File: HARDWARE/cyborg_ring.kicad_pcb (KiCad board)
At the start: 2 copper layers, 45 x 24.6 mm, 43 parts, among them SW1 SW_PUSH, U1 ATtiny85_QFN20_1-5, U2 ATtiny85_QFN20_11-15

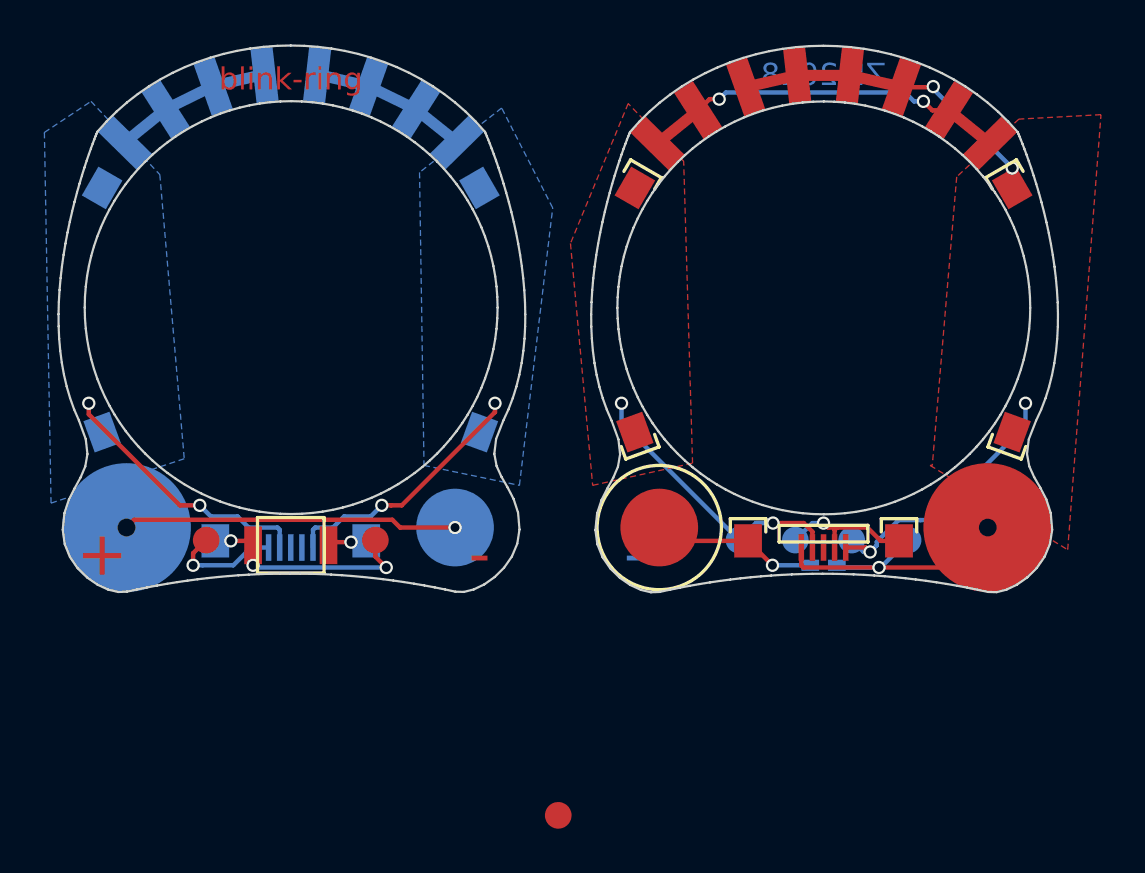
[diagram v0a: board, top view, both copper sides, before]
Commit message: localized schematic symbols. changed name. minor formatting changes.
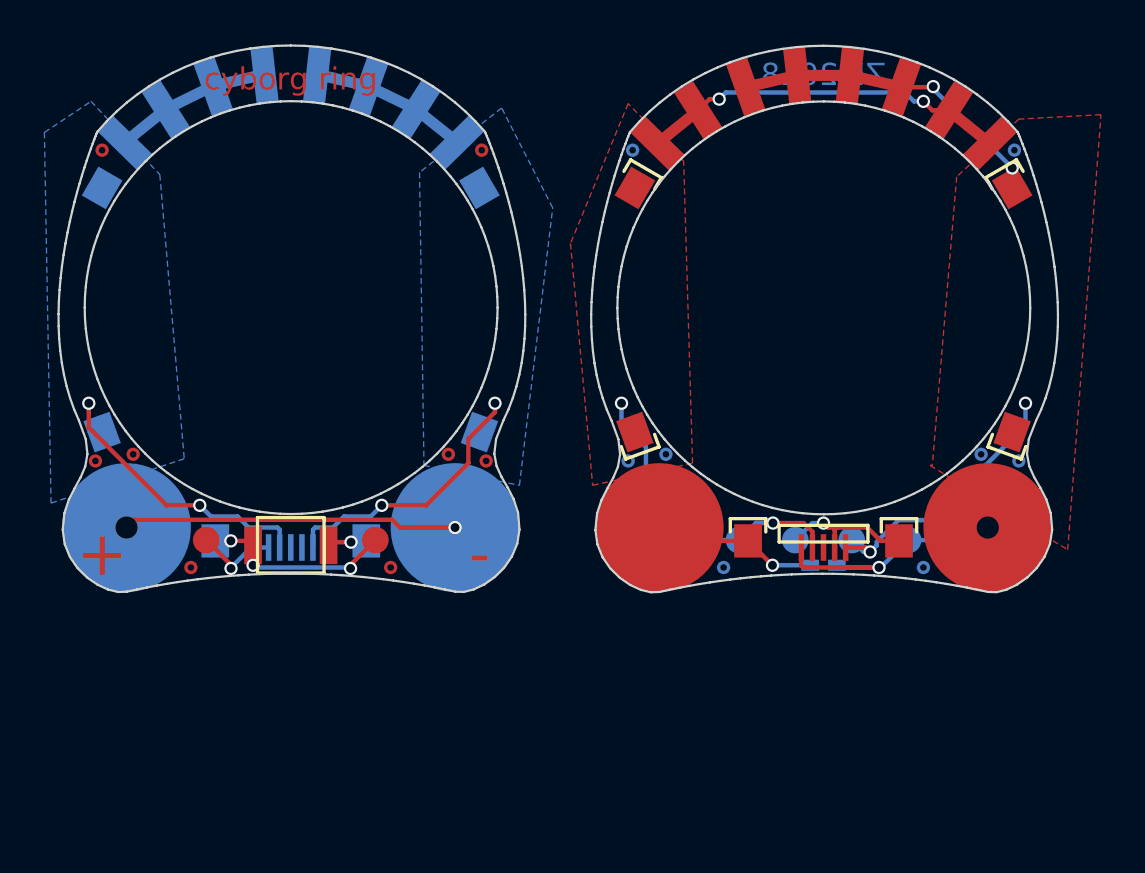
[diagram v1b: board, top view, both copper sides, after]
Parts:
- removed TP6: GND, KiCad_Footprints:ZF_CONN_1-2_pad
- added REF**: ZF_STRUCT_HOLE_0-30mm, KiCad_Footprints:ZF_STRUCT_HOLE_0-30mm, B.Cu at (98.6, 132.8)
- added REF**: ZF_STRUCT_HOLE_0-30mm, KiCad_Footprints:ZF_STRUCT_HOLE_0-30mm, F.Cu at (57.2, 146.8)
- added REF**: ZF_STRUCT_HOLE_0-30mm, KiCad_Footprints:ZF_STRUCT_HOLE_0-30mm, F.Cu at (58.9, 146.5)
- added REF**: ZF_STRUCT_HOLE_0-30mm, KiCad_Footprints:ZF_STRUCT_HOLE_0-30mm, F.Cu at (73.1, 146.5)
- added REF**: ZF_STRUCT_HOLE_0-30mm, KiCad_Footprints:ZF_STRUCT_HOLE_0-30mm, F.Cu at (74.8, 146.8)
- added REF**: ZF_STRUCT_HOLE_0-30mm, KiCad_Footprints:ZF_STRUCT_HOLE_0-30mm, B.Cu at (81.2, 146.8)
- added REF**: ZF_STRUCT_HOLE_0-30mm, KiCad_Footprints:ZF_STRUCT_HOLE_0-30mm, B.Cu at (82.9, 146.5)
- added REF**: ZF_STRUCT_HOLE_0-30mm, KiCad_Footprints:ZF_STRUCT_HOLE_0-30mm, B.Cu at (98.8, 146.8)
- added REF**: ZF_STRUCT_HOLE_0-30mm, KiCad_Footprints:ZF_STRUCT_HOLE_0-30mm, B.Cu at (97.1, 146.5)
- added REF**: ZF_STRUCT_HOLE_0-30mm, KiCad_Footprints:ZF_STRUCT_HOLE_0-30mm, F.Cu at (57.5, 132.8)
- added REF**: ZF_STRUCT_HOLE_0-30mm, KiCad_Footprints:ZF_STRUCT_HOLE_0-30mm, F.Cu at (74.6, 132.8)
- added REF**: ZF_STRUCT_HOLE_0-30mm, KiCad_Footprints:ZF_STRUCT_HOLE_0-30mm, B.Cu at (81.4, 132.8)
- added REF**: ZF_STRUCT_HOLE_0-30mm, KiCad_Footprints:ZF_STRUCT_HOLE_0-30mm, F.Cu at (61.5, 151.6)
- added REF**: ZF_STRUCT_HOLE_0-30mm, KiCad_Footprints:ZF_STRUCT_HOLE_0-30mm, F.Cu at (70.5, 151.6)
- added REF**: ZF_STRUCT_HOLE_0-30mm, KiCad_Footprints:ZF_STRUCT_HOLE_0-30mm, B.Cu at (85.5, 151.6)
- added REF**: ZF_STRUCT_HOLE_0-30mm, KiCad_Footprints:ZF_STRUCT_HOLE_0-30mm, B.Cu at (94.5, 151.6)
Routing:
- net VCC: track 13.7 -> 11.9 mm
- net Net-(NA3-Pad1): track 10.2 -> 8.88 mm
- net Net-(TP1-Pad1): track 5.11 -> 3.85 mm
- net /LED_BOTTOM_1: track 18.7 -> 19.4 mm
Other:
- board text added: "cyborg ring"
- board text removed: "blink-ring"

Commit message: added 10M+10M R0805+R0805 reinforcement resistors to BOM and schematic. updated component references on schematic, BOM, and layout to start with 'BOT_' or 'TOP_' for cordwood-style installations. minor schematic readability improvements.
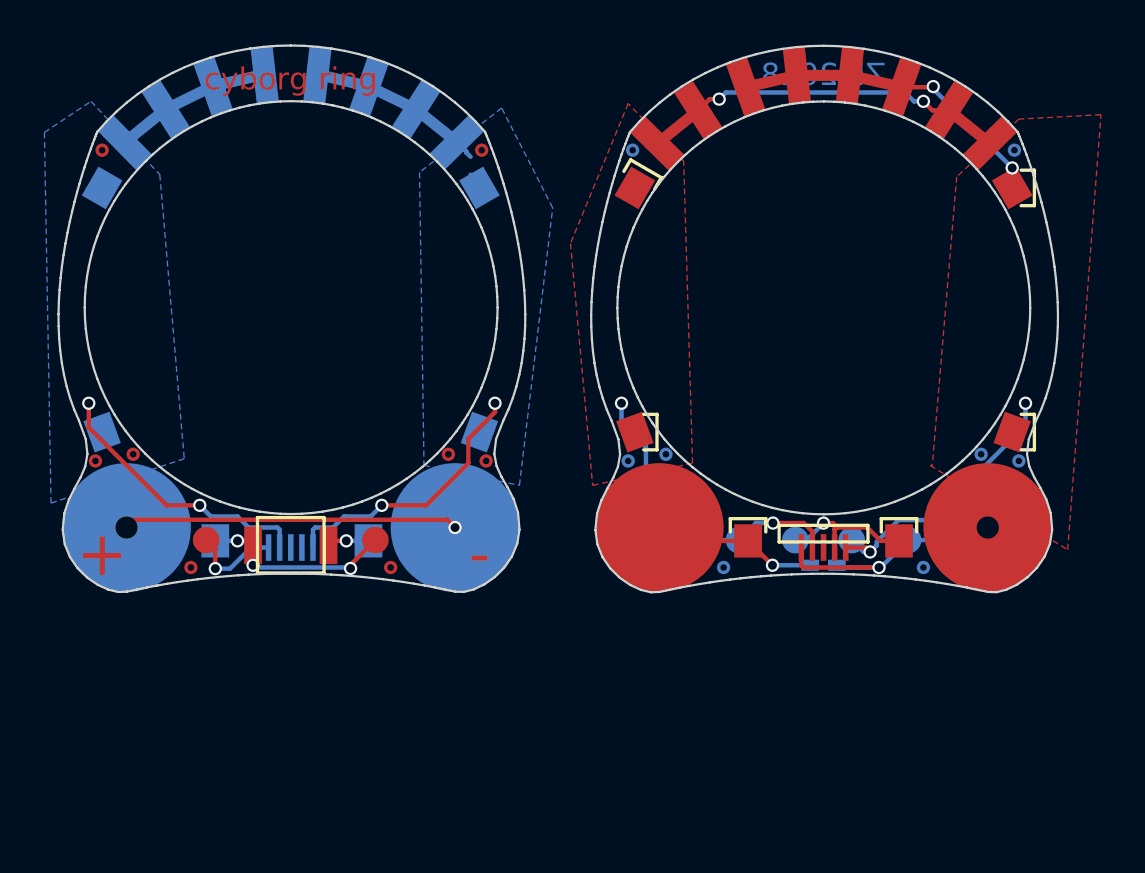
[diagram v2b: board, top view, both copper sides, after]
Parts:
- removed D1, R5: LED0, KiCad_Footprints:ZF_SMD_0508_CORD
- removed D2, R6: LED1, KiCad_Footprints:ZF_SMD_0508_CORD
- removed D3, R7: LED2, KiCad_Footprints:ZF_SMD_0508_CORD
- removed D4, R8: LED3, KiCad_Footprints:ZF_SMD_0508_CORD
- removed D5, R9: LED4, KiCad_Footprints:ZF_SMD_0508_CORD
- removed D6, R10: LED5, KiCad_Footprints:ZF_SMD_0508_CORD
- removed D7, R11: LED6, KiCad_Footprints:ZF_SMD_0508_CORD
- removed D8, R12: LED7, KiCad_Footprints:ZF_SMD_0508_CORD
- removed NA1, NA2: SW_JMP, KiCad_Footprints:ZF_SMD_0805_CORD
- removed NA3, NA4: JMP_GND, KiCad_Footprints:ZF_SMD_0805_CORD
- removed R1: BATT0-, KiCad_Footprints:ZF_BATT_AC10E_NEG
- removed R2: BATT0+, KiCad_Footprints:ZF_BATT_AC10E_POS
- removed R3: BATT1+, KiCad_Footprints:ZF_BATT_AC10E_POS
- removed R4: BATT1-, KiCad_Footprints:ZF_BATT_AC10E_NEG
- removed the REF** at (98.5, 134.5)
- removed the REF** at (98.5, 145.5)
- removed the REF** at (74.5, 145.5)
- removed the REF** at (57.5, 145.5)
- removed the REF** at (81.5, 145.5)
- removed the REF** at (57.5, 134.5)
- removed the REF** at (74.5, 134.5)
- removed the REF** at (81.5, 134.5)
- removed U1: ATtiny85_QFN20_1-5, KiCad_Footprints:ZF_IC_MLF20-050_CORD_1-5
- removed U2: ATtiny85_QFN20_11-15, KiCad_Footprints:ZF_IC_MLF20-050_CORD_11-15
- added BOT_D1: 22R+LED+22R, KiCad_Footprints:ZF_SMD_0508_CORD, B.Cu at (58.5, 132.5)
- added BOT_D2: 22R+LED+22R, KiCad_Footprints:ZF_SMD_0508_CORD, B.Cu at (60.4, 131.0)
- added BOT_D3: 22R+LED+22R, KiCad_Footprints:ZF_SMD_0508_CORD, B.Cu at (62.5, 129.9)
- added BOT_D4: 22R+LED+22R, KiCad_Footprints:ZF_SMD_0508_CORD, B.Cu at (64.8, 129.4)
- added BOT_D5: 22R+LED+22R, KiCad_Footprints:ZF_SMD_0508_CORD, B.Cu at (67.2, 129.4)
- added BOT_D6: 22R+LED+22R, KiCad_Footprints:ZF_SMD_0508_CORD, B.Cu at (69.5, 129.9)
- added BOT_D7: 22R+LED+22R, KiCad_Footprints:ZF_SMD_0508_CORD, B.Cu at (71.6, 131.0)
- added BOT_D8: 22R+LED+22R, KiCad_Footprints:ZF_SMD_0508_CORD, B.Cu at (73.5, 132.4)
- added BOT_PAD1: BATT0-, KiCad_Footprints:ZF_BATT_AC10E_NEG, B.Cu at (73.4, 149.8)
- added BOT_PAD2: BATT1+, KiCad_Footprints:ZF_BATT_AC10E_POS, B.Cu at (58.6, 149.8)
- added BOT_R1: JMP+JMP, KiCad_Footprints:ZF_SMD_0805_CORD, B.Cu at (69.5, 150.4)
- added BOT_R2: JMP+JMP, KiCad_Footprints:ZF_SMD_0805_CORD, B.Cu at (62.6, 150.4)
- added BOT_R3: 10M+10M, KiCad_Footprints:ZF_SMD_0805_CORD, B.Cu at (57.5, 145.5)
- added BOT_R4: 10M+10M, KiCad_Footprints:ZF_SMD_0805_CORD, B.Cu at (74.5, 145.5)
- added BOT_R5: 10M+10M, KiCad_Footprints:ZF_SMD_0805_CORD, B.Cu at (57.5, 134.5)
- added BOT_R6: 10M+10M, KiCad_Footprints:ZF_SMD_0805_CORD, B.Cu at (74.5, 134.5)
- added BOT_U1: ATtiny85_QFN20_1-5, KiCad_Footprints:ZF_IC_MLF20-050_CORD_1-5, B.Cu at (66.0, 150.2)
- added TOP_D1: 22R+LED+22R, KiCad_Footprints:ZF_SMD_0508_CORD, F.Cu at (82.5, 132.5)
- added TOP_D2: 22R+LED+22R, KiCad_Footprints:ZF_SMD_0508_CORD, F.Cu at (84.4, 131.0)
- added TOP_D3: 22R+LED+22R, KiCad_Footprints:ZF_SMD_0508_CORD, F.Cu at (86.5, 130.0)
- added TOP_D4: 22R+LED+22R, KiCad_Footprints:ZF_SMD_0508_CORD, F.Cu at (88.8, 129.4)
- added TOP_D5: 22R+LED+22R, KiCad_Footprints:ZF_SMD_0508_CORD, F.Cu at (91.2, 129.4)
- added TOP_D6: 22R+LED+22R, KiCad_Footprints:ZF_SMD_0508_CORD, F.Cu at (93.5, 130.0)
- added TOP_D7: 22R+LED+22R, KiCad_Footprints:ZF_SMD_0508_CORD, F.Cu at (95.6, 131.0)
- added TOP_D8: 22R+LED+22R, KiCad_Footprints:ZF_SMD_0508_CORD, F.Cu at (97.5, 132.5)
- added TOP_PAD1: BATT0+, KiCad_Footprints:ZF_BATT_AC10E_POS, F.Cu at (97.4, 149.8)
- added TOP_PAD2: BATT1-, KiCad_Footprints:ZF_BATT_AC10E_NEG, F.Cu at (82.6, 149.8)
- added TOP_R1: JMP+JMP, KiCad_Footprints:ZF_SMD_0805_CORD, F.Cu at (93.4, 150.4)
- added TOP_R2: JMP+JMP, KiCad_Footprints:ZF_SMD_0805_CORD, F.Cu at (86.6, 150.4)
- added TOP_R3: 10M+10M, KiCad_Footprints:ZF_SMD_0805_CORD, F.Cu at (81.5, 145.5)
- added TOP_R4: 10M+10M, KiCad_Footprints:ZF_SMD_0805_CORD, F.Cu at (98.5, 145.5)
- added TOP_R5: 10M+10M, KiCad_Footprints:ZF_SMD_0805_CORD, F.Cu at (81.5, 134.5)
- added TOP_R6: 10M+10M, KiCad_Footprints:ZF_SMD_0805_CORD, F.Cu at (98.5, 134.5)
- added TOP_U1: ATtiny85_QFN20_11-15, KiCad_Footprints:ZF_IC_MLF20-050_CORD_11-15, F.Cu at (90.0, 150.2)
- C1: value C -> 0u1
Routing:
- net Net-(R1-Pad1): track 15.1 -> 0.00 mm, vias 1 -> 0
- net Net-(BOT_PAD1-Pad1): track 0.00 -> 15.1 mm, vias 0 -> 1
- net /LED_BOTTOM_1: track 19.4 -> 21.1 mm
